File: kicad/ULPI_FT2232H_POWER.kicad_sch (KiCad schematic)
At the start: 115 parts, among them J3 USB_B_RECEPTACLE, J4 USB_C_Receptacle, U10 LP5907MFX-3.3, U11 FT2232HQ, U12 TLV62569DBVT, U13 93LCxxBxxOT, U14 TLV62569DBVT, U15 TLV62569DBVT, U7 LP5907MFX-1.8, U8 USBLC6-2SC6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

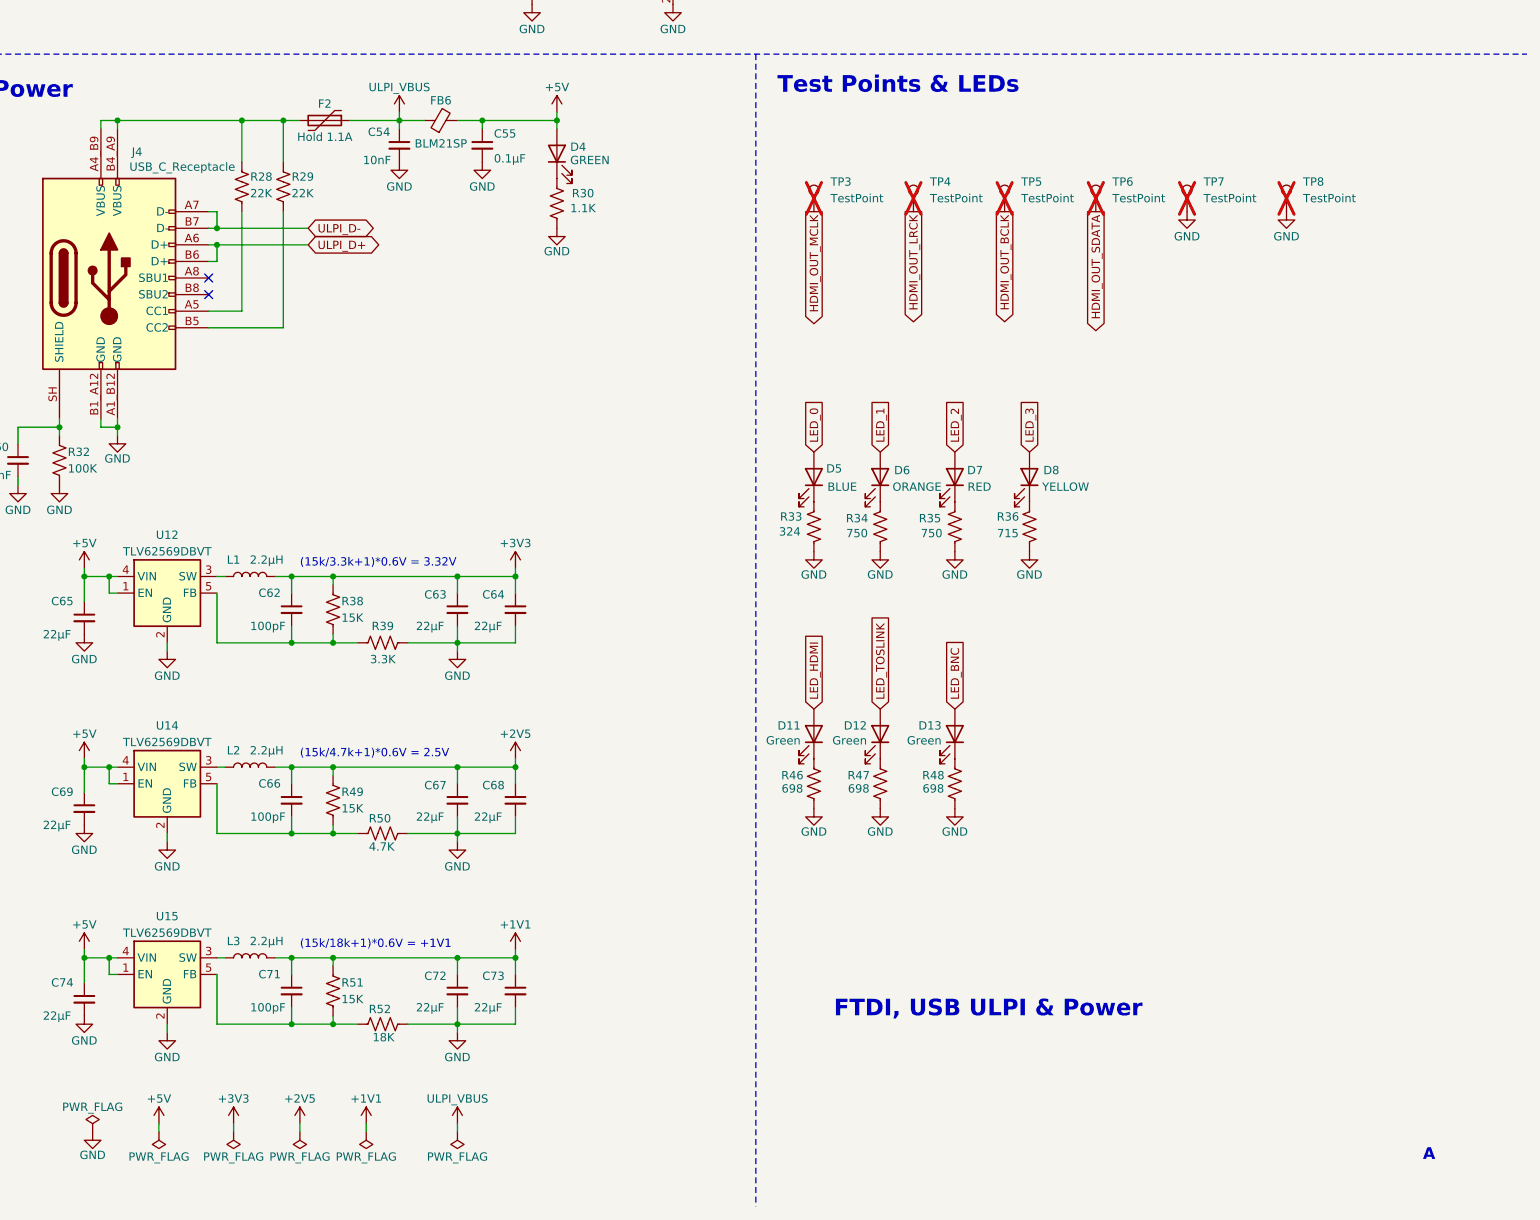
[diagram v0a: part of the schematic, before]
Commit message: 5.1K USB resistors
Replaces 22K resistors to VBUS with 5.1K resistors to GND.
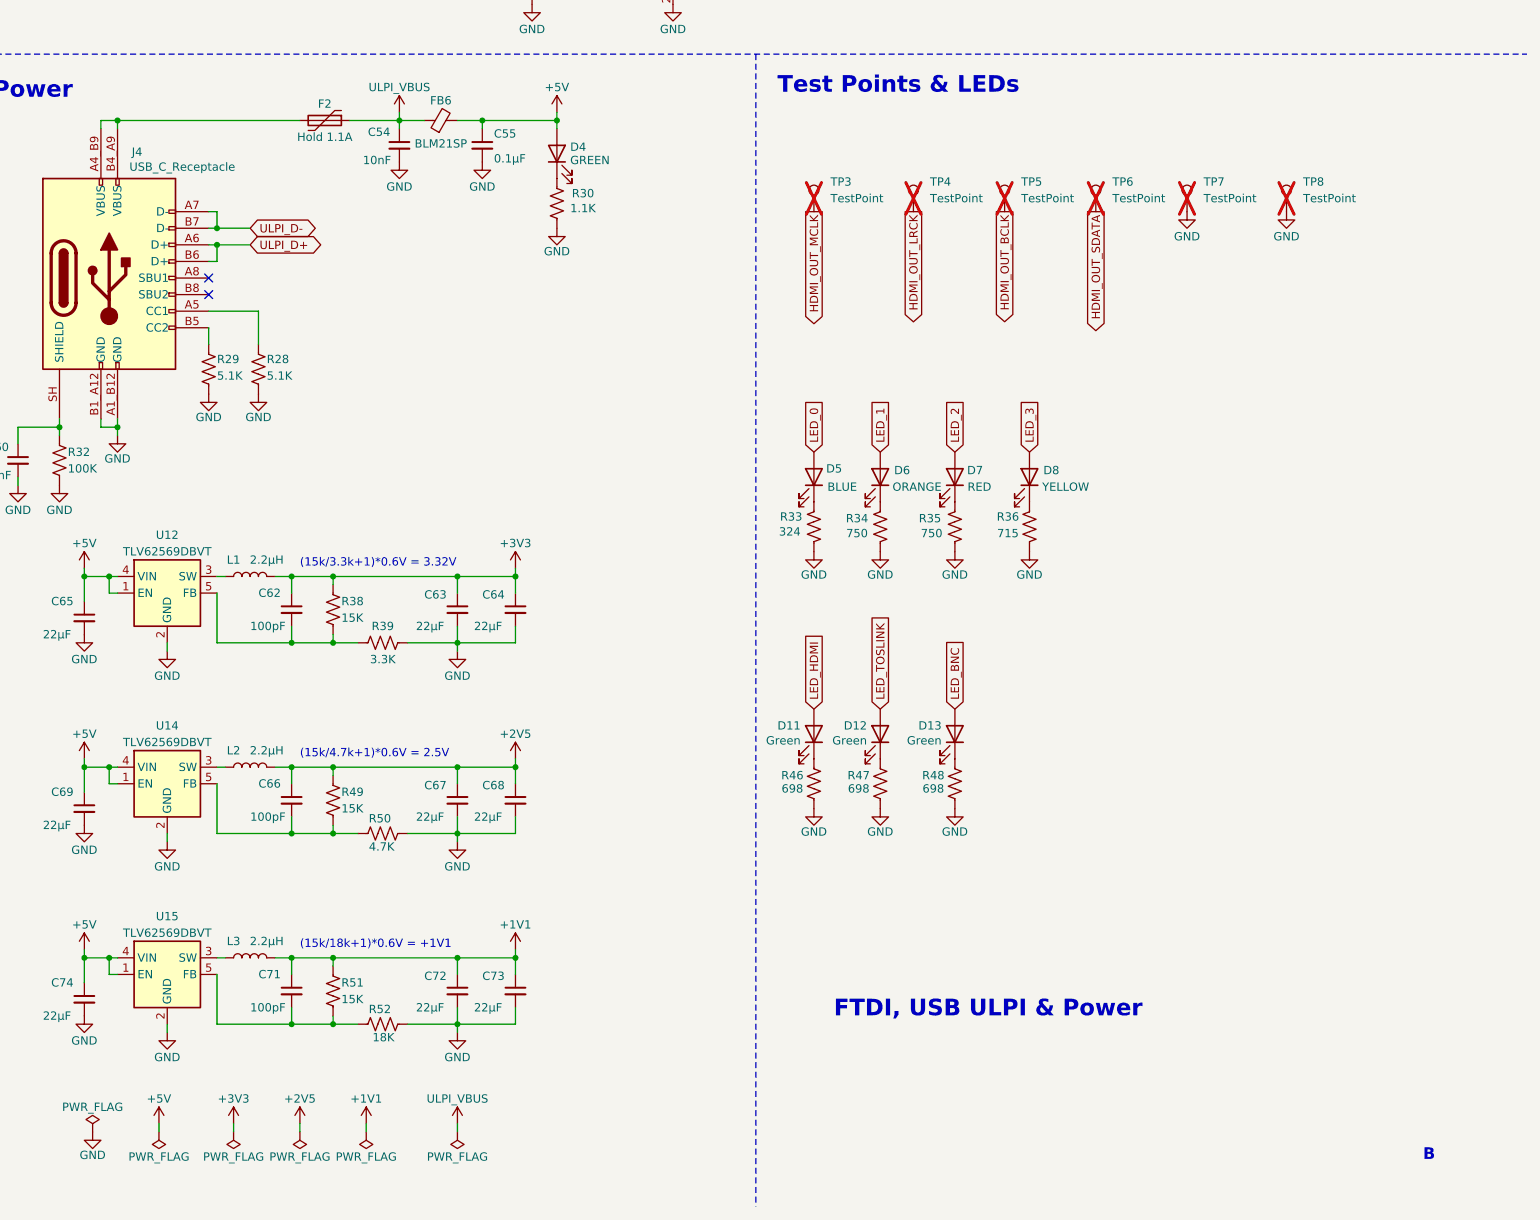
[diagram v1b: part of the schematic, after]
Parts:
- R28, R29: value 22K -> 5.1K; MPN ERJ-3EKF2202V -> ERJ-3EKF5101V
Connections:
- net GND: now also R28.2, R29.2
- net at F2.2, J4.A4_B9 (VBUS), J4.B4_A9 (VBUS): no longer R28.1, R29.1
- net at J4.A5 (CC1): now also R28.1; no longer R28.2
- net at J4.B5 (CC2): now also R29.1; no longer R29.2
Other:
- note added: "B"
- note removed: "A"
- moved on the sheet: R28, R29
